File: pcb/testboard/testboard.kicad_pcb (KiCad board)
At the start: 2 copper layers, 71.9 x 54.6 mm, 24 parts, among them IC1 TLE94112ESXUMA1, IC2 AP63203WU-7, J1 Left Socket, J2 Right Socket, J3 52207-0633, J4 52207-0633, J5 52207-0633, J6 USB_C_Receptacle_USB2.0_14P, SW1 Control, U1 CYPD3177-24LQXQ

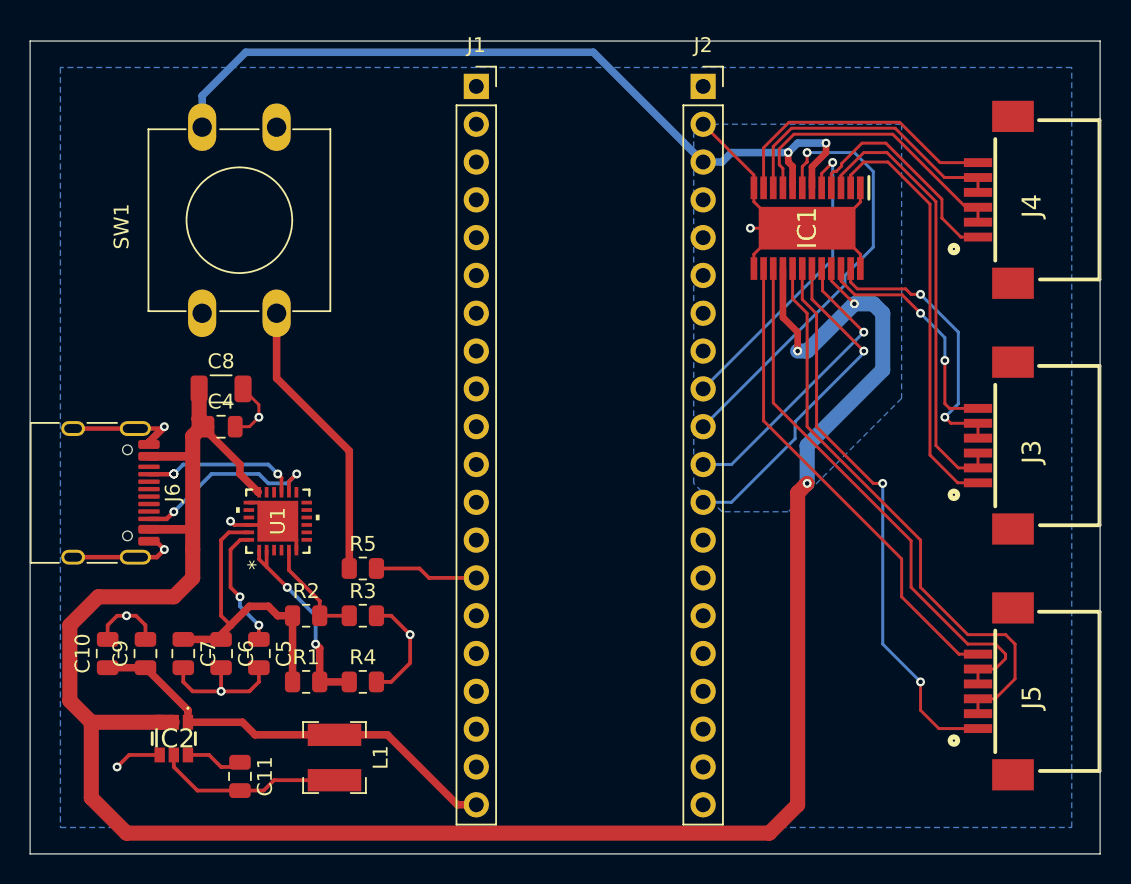
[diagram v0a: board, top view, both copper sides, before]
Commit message: Testboard errors resolved
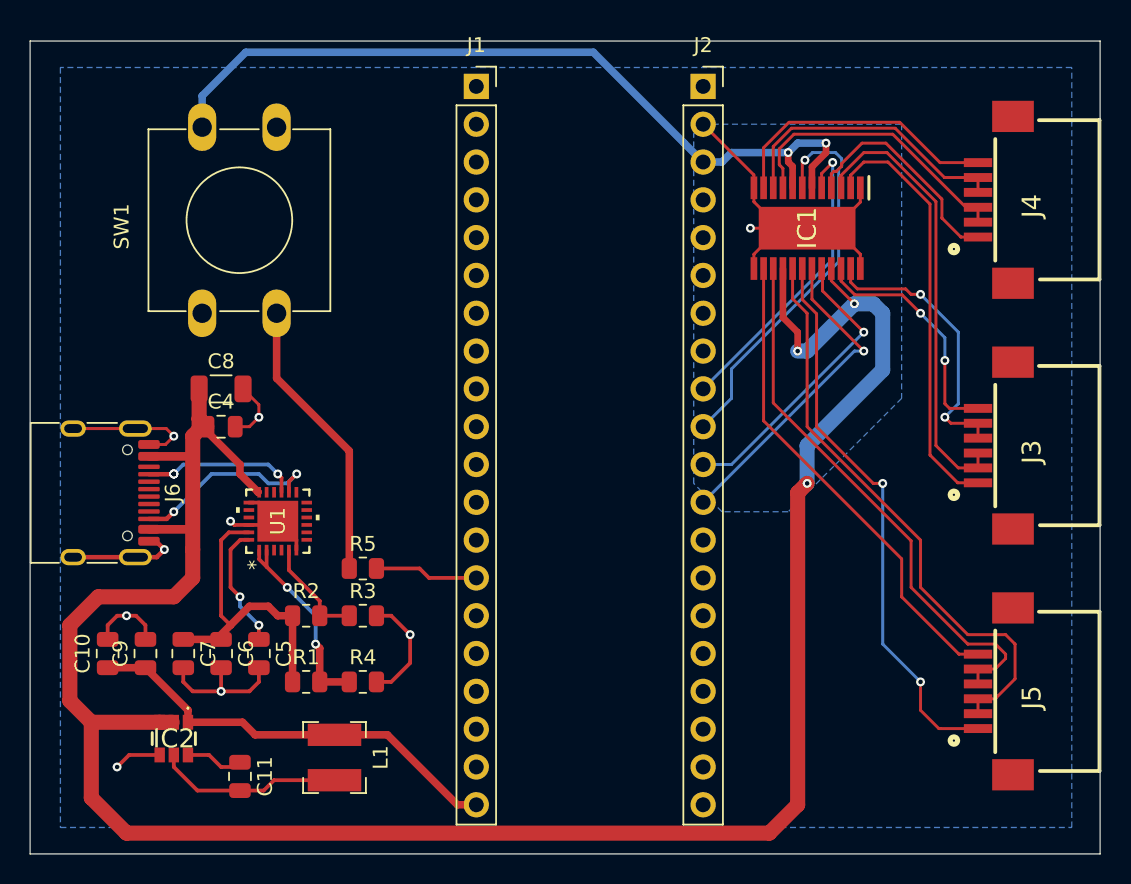
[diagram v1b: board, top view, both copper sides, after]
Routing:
- net /PA6: track 29.5 -> 26.8 mm
- net GND: track 81.7 -> 82.7 mm
- net /9V: track 157.4 -> 156.9 mm
